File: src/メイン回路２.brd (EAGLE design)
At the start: 3.8 x 15.2 mm, 26 parts

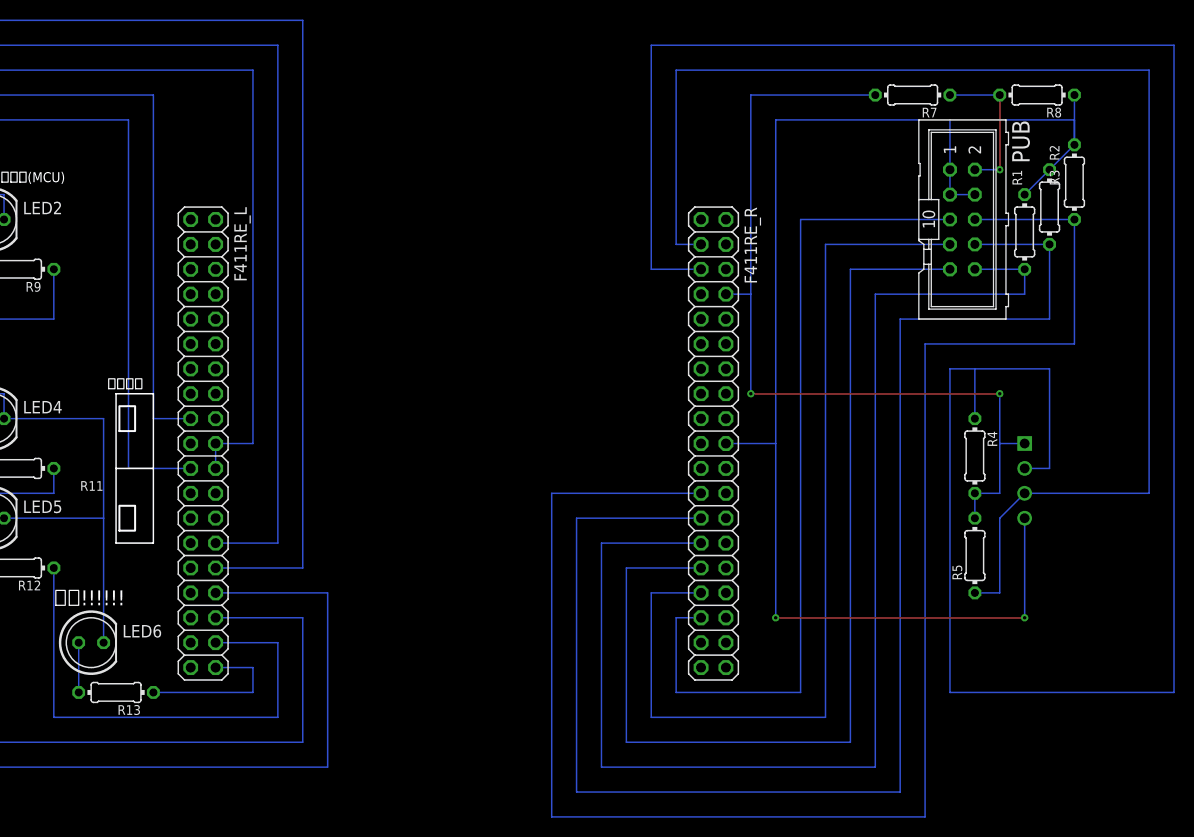
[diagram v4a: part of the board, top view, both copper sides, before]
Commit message: [complete]メイン回路2に暴走対策回路を追加
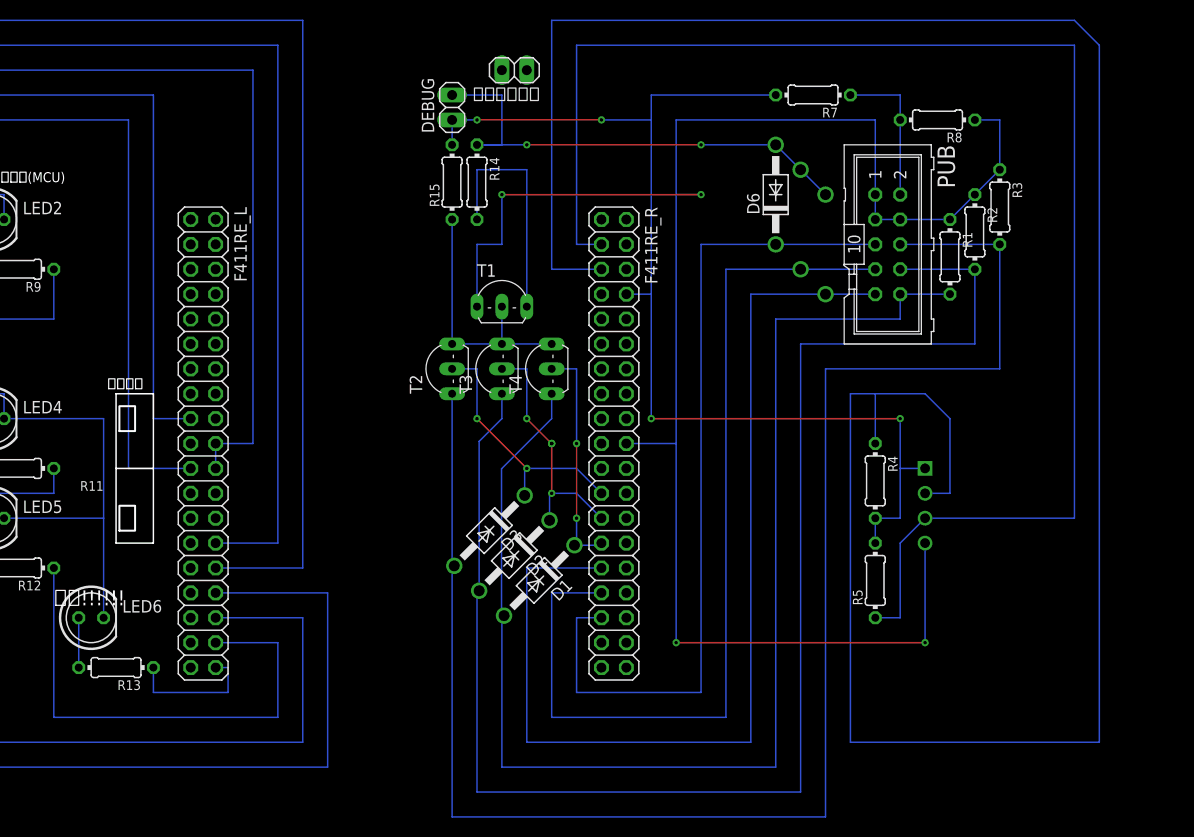
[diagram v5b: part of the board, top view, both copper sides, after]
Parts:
- added D1, D2, D3, D4, D5, D6: 1N4004, diode:DO41-10
- added DEBUG, ソケット置き: (no value), pinhead:1X02
- added R14, R15: 10k, rcl:0204/7
- added T1, T2, T3, T4: 一般的なトランジスタ, 一般的なトランジスタ:TO92-CEB
- moved MDC 10.5 mm to (111.8, 20.3)
- moved R4 10.5 mm to (106.7, 22.9)
- moved R5 10.5 mm to (106.7, 12.7)
- moved R8 10.5 mm to (113.0, 59.7)
- moved F411RE_R 10.2 mm to (80.0, 26.7)
- moved R7 10.2 mm to (100.3, 62.2)
- moved U$2 10.2 mm to (132.1, -19.1)
- moved R3 8.03 mm to (119.4, 50.8)
- moved R1 8.03 mm to (114.3, 45.7)
- moved PUB 8.03 mm to (108.0, 47.0)
- moved R2 8.03 mm to (116.8, 48.3)
- moved LED6 2.54 mm to (26.7, 8.89)
- moved R13 2.54 mm to (29.2, 3.81)
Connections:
- new net DEBUG: D4.A, D5.A, D6.A, DEBUG.2, R14.1
- new net N$7: R14.2, T1.B
- new net N$8: D1.A, PUB.10, R1.2, T4.E
- new net N$9: D2.A, PUB.8, R2.2, T3.E
- new net N$Q0: D3.A, PUB.6, R3.2, T2.E
- new net ZM: R15.1, T1.C, T2.B, T3.B, T4.B
- net DIR1: now also D4.C
- net DIR2: now also D5.C
- net DIR3: now also D6.C
- net GND: now also T1.E
- net PWM1: now also D1.C, T4.C; no longer PUB.10, R1.2
- net PWM2: now also D2.C, T3.C; no longer PUB.8, R2.2
- net PWM3: now also D3.C, T2.C; no longer PUB.6, R3.2
- net U5V: now also DEBUG.1, R15.2
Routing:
- net N$Q0: track 0.00 -> 167.8 mm
- net N$9: track 0.00 -> 153.5 mm
- net PWM3: track 172.7 -> 26.6 mm, vias 0 -> 2
- net N$8: track 0.00 -> 134.4 mm
- net PWM2: track 152.4 -> 25.6 mm, vias 0 -> 4
- net PWM1: track 132.1 -> 23.5 mm, vias 0 -> 2
- net DEBUG: track 0.00 -> 50.4 mm, vias 0 -> 2
- net GND: track 343.7 -> 378.0 mm, vias 2 -> 4
- net ZM: track 0.00 -> 26.7 mm
- net U5V: track 88.9 -> 114.3 mm, vias 2 -> 4
- net N$7: track 0.00 -> 24.1 mm
- net SDA: track 231.1 -> 245.9 mm
- net SCL: track 138.2 -> 150.9 mm
- net LED6: track 16.5 -> 14.0 mm
- net 3V: vias 1 -> 0
